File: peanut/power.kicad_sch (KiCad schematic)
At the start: 17 parts, among them J3 Battery JST, J4 Arming, Q5 PMOS, U4 TLV75733PDBVR, U5 TPS2116DRL

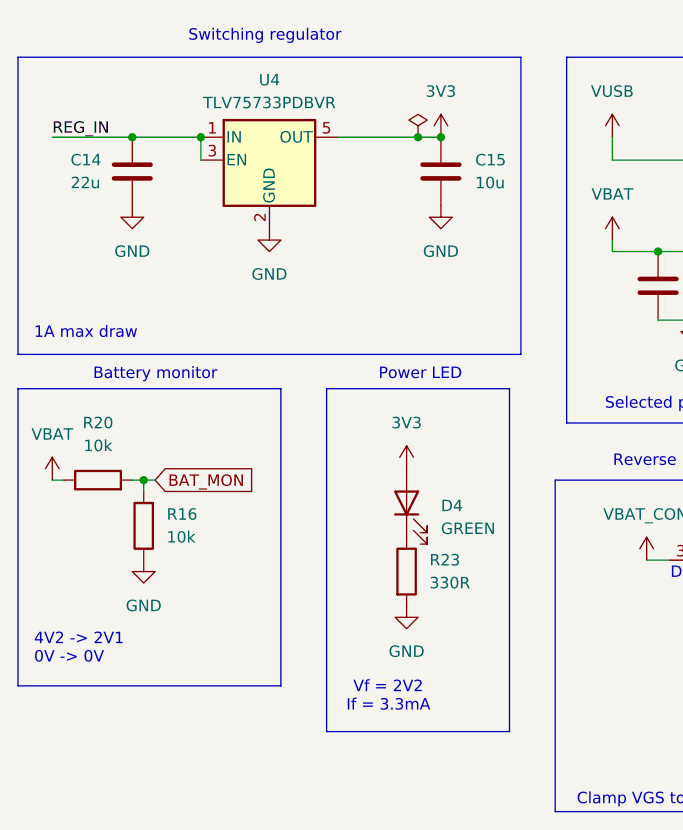
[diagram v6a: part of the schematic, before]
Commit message: feat: change LDO again to something with better dropout voltage
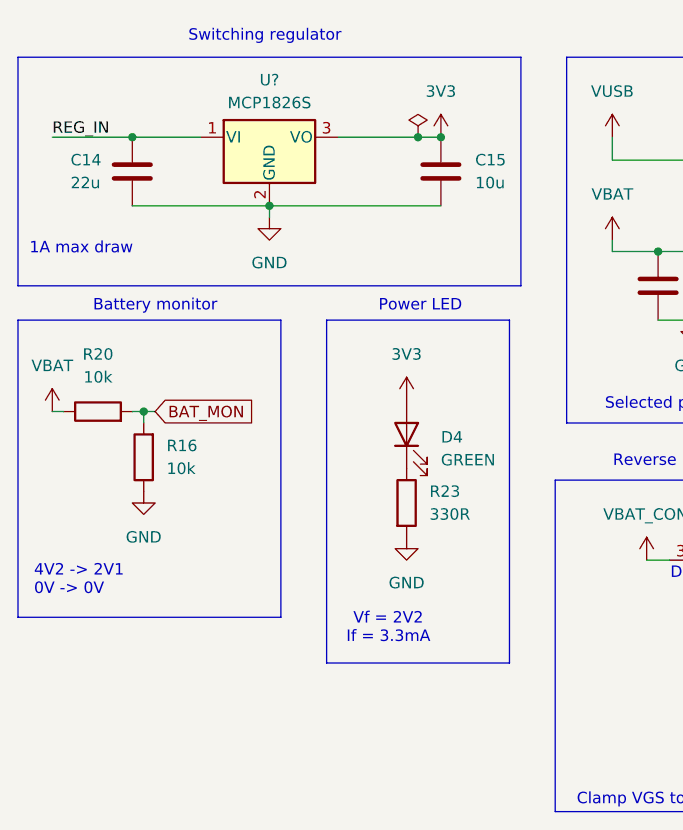
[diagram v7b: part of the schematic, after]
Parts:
- removed U4: TLV75733PDBVR, Package_TO_SOT_SMD:SOT-23-5, symbol Regulator_Linear:TLV75733PDBV
- added U?: MCP1826S, Package_TO_SOT_SMD:SOT-223-3_TabPin2, symbol Regulator_Linear:MCP1826S
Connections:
- net 3V3: now also U?.3 (VO)
- net GND: now also U?.2 (GND)
- net REG_IN: now also U?.1 (VI)
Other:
- moved on the sheet: D4, R16, R20, R23

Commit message: chore: re-annotate
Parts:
- gave numbers to parts that had none: 1
- renumbered C14 to C15, C15 to C16, C16 to C17, C17 to C18, C18 to C19, D4 to D5, R16 to R21, R23 to R22, R17 to R23
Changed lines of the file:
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@@
 		(dnp no)
 		(fields_autoplaced yes)
-		(property "Reference" "R16"
+		(property "Reference" "R21"
 			(at 55.88 102.8699 0)
 			(show_name no)
@@
 			(project "peanut"
 				(path "/5c6b6cfc-6c84-425a-9b66-e6111713aae8/f944ce75-1da7-4030-9ed2-502ac98b17ed"
-					(reference "R16")
+					(reference "R21")
 					(unit 1)
 				)
@@
 		(dnp no)
 		(fields_autoplaced yes)
-		(property "Reference" "C16"
+		(property "Reference" "C17"
 			(at 114.3 83.8199 0)
 			(show_name no)
@@
 			(project "peanut"
 				(path "/5c6b6cfc-6c84-425a-9b66-e6111713aae8/f944ce75-1da7-4030-9ed2-502ac98b17ed"
-					(reference "C16")
+					(reference "C17")
 					(unit 1)
 				)
@@
 		(dnp no)
 		(fields_autoplaced yes)
-		(property "Reference" "#PWR059"
+		(property "Reference" "#PWR058"
 			(at 232.41 80.01 0)
 			(hide yes)
@@
 			(project "peanut"
 				(path "/5c6b6cfc-6c84-425a-9b66-e6111713aae8/f944ce75-1da7-4030-9ed2-502ac98b17ed"
-					(reference "#PWR059")
+					(reference "#PWR058")
 					(unit 1)
 				)
@@
 		(dnp no)
 		(fields_autoplaced yes)
-		(property "Reference" "#PWR051"
+		(property "Reference" "#PWR054"
 			(at 163.83 77.47 0)
 			(hide yes)
@@
 			(project "peanut"
 				(path "/5c6b6cfc-6c84-425a-9b66-e6111713aae8/f944ce75-1da7-4030-9ed2-502ac98b17ed"
-					(reference "#PWR051")
+					(reference "#PWR054")
 					(unit 1)
 				)
@@
 		(dnp no)
 		(fields_autoplaced yes)
-		(property "Reference" "#PWR050"
+		(property "Reference" "#PWR053"
 			(at 139.7 92.71 0)
 			(hide yes)
@@
 			(project "peanut"
 				(path "/5c6b6cfc-6c84-425a-9b66-e6111713aae8/f944ce75-1da7-4030-9ed2-502ac98b17ed"
-					(reference "#PWR050")
+					(reference "#PWR053")
 					(unit 1)
 				)
@@
 		(in_pos_files yes)
 		(dnp no)
-		(property "Reference" "#PWR060"
+		(property "Reference" "#PWR057"
 			(at 231.14 71.12 0)
 			(hide yes)
@@
 			(project "peanut"
 				(path "/5c6b6cfc-6c84-425a-9b66-e6111713aae8/f944ce75-1da7-4030-9ed2-502ac98b17ed"
-					(reference "#PWR060")
+					(reference "#PWR057")
 					(unit 1)
 				)
@@
 		(dnp no)
 		(fields_autoplaced yes)
-		(property "Reference" "#FLG01"
+		(property "Reference" "#FLG05"
 			(at 227.33 67.945 0)
 			(hide yes)
@@
 			(project "peanut"
 				(path "/5c6b6cfc-6c84-425a-9b66-e6111713aae8/f944ce75-1da7-4030-9ed2-502ac98b17ed"
-					(reference "#FLG01")
+					(reference "#FLG05")
 					(unit 1)
 				)
@@
 		(dnp no)
 		(fields_autoplaced yes)
-		(property "Reference" "#PWR052"
+		(property "Reference" "#PWR051"
 			(at 116.84 140.97 0)
 			(hide yes)
@@
 			(project "peanut"
 				(path "/5c6b6cfc-6c84-425a-9b66-e6111713aae8/f944ce75-1da7-4030-9ed2-502ac98b17ed"
-					(reference "#PWR052")
+					(reference "#PWR051")
 					(unit 1)
 				)
@@
 		(dnp no)
 		(fields_autoplaced yes)
-		(property "Reference" "#PWR035"
+		(property "Reference" "#PWR056"
 			(at 199.39 71.12 0)
 			(hide yes)
@@
 			(project "peanut"
 				(path "/5c6b6cfc-6c84-425a-9b66-e6111713aae8/f944ce75-1da7-4030-9ed2-502ac98b17ed"
-					(reference "#PWR035")
+					(reference "#PWR056")
 					(unit 1)
 				)
@@
 		(dnp no)
 		(fields_autoplaced yes)
-		(property "Reference" "#FLG05"
+		(property "Reference" "#FLG04"
 			(at 196.85 65.405 0)
 			(hide yes)
@@
 			(project "peanut"
 				(path "/5c6b6cfc-6c84-425a-9b66-e6111713aae8/f944ce75-1da7-4030-9ed2-502ac98b17ed"
-					(reference "#FLG05")
+					(reference "#FLG04")
 					(unit 1)
 				)
@@
 		(in_pos_files yes)
 		(dnp no)
-		(property "Reference" "C14"
+		(property "Reference" "C15"
 			(at 45.212 71.12 0)
 			(show_name no)
@@
 			(project "peanut"
 				(path "/5c6b6cfc-6c84-425a-9b66-e6111713aae8/f944ce75-1da7-4030-9ed2-502ac98b17ed"
-					(reference "C14")
+					(reference "C15")
 					(unit 1)
 				)
@@
 		(in_pos_files yes)
 		(dnp no)
-		(property "Reference" "#PWR039"
+		(property "Reference" "#PWR041"
 			(at 43.18 102.87 0)
 			(hide yes)
@@
 			(project "peanut"
 				(path "/5c6b6cfc-6c84-425a-9b66-e6111713aae8/f944ce75-1da7-4030-9ed2-502ac98b17ed"
-					(reference "#PWR039")
+					(reference "#PWR041")
 					(unit 1)
 				)
@@
 		(dnp no)
 		(fields_autoplaced yes)
-		(property "Reference" "C17"
+		(property "Reference" "C18"
 			(at 121.92 73.6599 0)
 			(show_name no)
@@
 			(project "peanut"
 				(path "/5c6b6cfc-6c84-425a-9b66-e6111713aae8/f944ce75-1da7-4030-9ed2-502ac98b17ed"
-					(reference "C17")
+					(reference "C18")
 					(unit 1)
 				)
@@
 		(dnp no)
 		(fields_autoplaced yes)
-		(property "Reference" "U?"
+		(property "Reference" "U4"
 			(at 67.31 62.23 0)
 			(show_name no)
@@
 			(project "peanut"
 				(path "/5c6b6cfc-6c84-425a-9b66-e6111713aae8/f944ce75-1da7-4030-9ed2-502ac98b17ed"
-					(reference "U?")
+					(reference "U4")
 					(unit 1)
 				)
@@
 		(dnp no)
 		(fields_autoplaced yes)
-		(property "Reference" "#PWR054"
+		(property "Reference" "#PWR055"
 			(at 198.12 76.2 0)
 			(hide yes)
@@
 			(project "peanut"
 				(path "/5c6b6cfc-6c84-425a-9b66-e6111713aae8/f944ce75-1da7-4030-9ed2-502ac98b17ed"
-					(reference "#PWR054")
+					(reference "#PWR055")
 					(unit 1)
 				)
@@
 		(dnp no)
 		(fields_autoplaced yes)
-		(property "Reference" "#PWR053"
+		(property "Reference" "#PWR052"
 			(at 127 119.38 0)
 			(hide yes)
@@
 			(project "peanut"
 				(path "/5c6b6cfc-6c84-425a-9b66-e6111713aae8/f944ce75-1da7-4030-9ed2-502ac98b17ed"
-					(reference "#PWR053")
+					(reference "#PWR052")
 					(unit 1)
 				)
@@
 		(dnp no)
 		(fields_autoplaced yes)
-		(property "Reference" "#PWR045"
+		(property "Reference" "#PWR046"
 			(at 86.36 72.39 0)
 			(hide yes)
@@
 			(project "peanut"
 				(path "/5c6b6cfc-6c84-425a-9b66-e6111713aae8/f944ce75-1da7-4030-9ed2-502ac98b17ed"
-					(reference "#PWR045")
+					(reference "#PWR046")
 					(unit 1)
 				)
@@
 		(in_pos_files yes)
 		(dnp no)
-		(property "Reference" "#PWR037"
+		(property "Reference" "#PWR049"
 			(at 109.22 119.38 0)
 			(hide yes)
@@
 			(project "peanut"
 				(path "/5c6b6cfc-6c84-425a-9b66-e6111713aae8/f944ce75-1da7-4030-9ed2-502ac98b17ed"
-					(reference "#PWR037")
+					(reference "#PWR049")
 					(unit 1)
 				)
@@
 		(dnp no)
 		(fields_autoplaced yes)
-		(property "Reference" "#PWR044"
+		(property "Reference" "#PWR045"
 			(at 82.55 119.38 0)
 			(hide yes)
@@
 			(project "peanut"
 				(path "/5c6b6cfc-6c84-425a-9b66-e6111713aae8/f944ce75-1da7-4030-9ed2-502ac98b17ed"
-					(reference "#PWR044")
+					(reference "#PWR045")
 					(unit 1)
 				)
@@
 		(dnp no)
 		(fields_autoplaced yes)
-		(property "Reference" "R17"
+		(property "Reference" "R23"
 			(at 119.38 129.5399 0)
 			(show_name no)
@@
 			(project "peanut"
 				(path "/5c6b6cfc-6c84-425a-9b66-e6111713aae8/f944ce75-1da7-4030-9ed2-502ac98b17ed"
-					(reference "R17")
+					(reference "R23")
 					(unit 1)
 				)
@@
 		(dnp no)
 		(fields_autoplaced yes)
-		(property "Reference" "C15"
+		(property "Reference" "C16"
 			(at 90.17 71.1199 0)
 			(show_name no)
@@
 			(project "peanut"
 				(path "/5c6b6cfc-6c84-425a-9b66-e6111713aae8/f944ce75-1da7-4030-9ed2-502ac98b17ed"
-					(reference "C15")
+					(reference "C16")
 					(unit 1)
 				)
@@
 		(dnp no)
 		(fields_autoplaced yes)
-		(property "Reference" "R23"
+		(property "Reference" "R22"
 			(at 85.09 107.9499 0)
 			(show_name no)
@@
 			(project "peanut"
 				(path "/5c6b6cfc-6c84-425a-9b66-e6111713aae8/f944ce75-1da7-4030-9ed2-502ac98b17ed"
-					(reference "R23")
+					(reference "R22")
 					(unit 1)
 				)
@@
 		(dnp no)
 		(fields_autoplaced yes)
-		(property "Reference" "#PWR041"
+		(property "Reference" "#PWR042"
 			(at 53.34 114.3 0)
 			(hide yes)
@@
 			(project "peanut"
 				(path "/5c6b6cfc-6c84-425a-9b66-e6111713aae8/f944ce75-1da7-4030-9ed2-502ac98b17ed"
-					(reference "#PWR041")
+					(reference "#PWR042")
 					(unit 1)
 				)
@@
 		(dnp no)
 		(fields_autoplaced yes)
-		(property "Reference" "#PWR043"
+		(property "Reference" "#PWR044"
 			(at 82.55 101.6 0)
 			(hide yes)
@@
 			(project "peanut"
 				(path "/5c6b6cfc-6c84-425a-9b66-e6111713aae8/f944ce75-1da7-4030-9ed2-502ac98b17ed"
-					(reference "#PWR043")
+					(reference "#PWR044")
 					(unit 1)
 				)
@@
 		(dnp no)
 		(fields_autoplaced yes)
-		(property "Reference" "#PWR042"
+		(property "Reference" "#PWR043"
 			(at 67.31 83.82 0)
 			(hide yes)
@@
 			(project "peanut"
 				(path "/5c6b6cfc-6c84-425a-9b66-e6111713aae8/f944ce75-1da7-4030-9ed2-502ac98b17ed"
-					(reference "#PWR042")
+					(reference "#PWR043")
 					(unit 1)
 				)
@@
 		(dnp no)
 		(fields_autoplaced yes)
-		(property "Reference" "#PWR049"
+		(property "Reference" "#PWR050"
 			(at 114.3 95.25 0)
 			(hide yes)
@@
 			(project "peanut"
 				(path "/5c6b6cfc-6c84-425a-9b66-e6111713aae8/f944ce75-1da7-4030-9ed2-502ac98b17ed"
-					(reference "#PWR049")
+					(reference "#PWR050")
 					(unit 1)
 				)
@@
 		(dnp no)
 		(fields_autoplaced yes)
-		(property "Reference" "C18"
+		(property "Reference" "C19"
 			(at 157.48 74.9299 0)
 			(show_name no)
@@
 			(project "peanut"
 				(path "/5c6b6cfc-6c84-425a-9b66-e6111713aae8/f944ce75-1da7-4030-9ed2-502ac98b17ed"
-					(reference "C18")
+					(reference "C19")
 					(unit 1)
 				)
@@
 		(dnp no)
 		(fields_autoplaced yes)
-		(property "Reference" "D4"
+		(property "Reference" "D5"
 			(at 86.36 101.9174 90)
 			(show_name no)
@@
 			(project "peanut"
 				(path "/5c6b6cfc-6c84-425a-9b66-e6111713aae8/f944ce75-1da7-4030-9ed2-502ac98b17ed"
-					(reference "D4")
+					(reference "D5")
 					(unit 1)
 				)
